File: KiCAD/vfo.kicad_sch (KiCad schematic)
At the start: 18 parts, among them Q1 J310, U1 Si5351A_Breakout, U2 MC1496

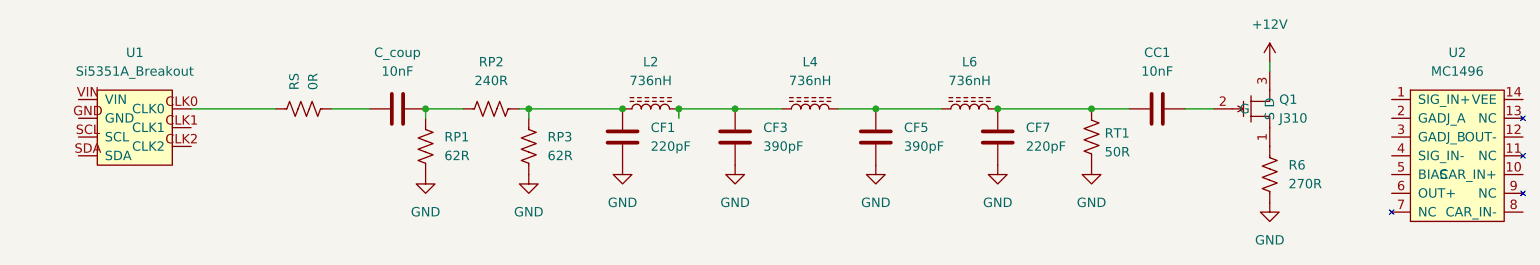
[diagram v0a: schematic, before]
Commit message: kicad: control-board sheets — buffer_keyer keyer body, arduino SPI labels, custom-symbol plan
- buffer_keyer.kicad_sch: place MC1496 keyer support components
  (carrier divider R11/R12, modulator port R3, emitter-degen Re,
  modulator coupling C1, VEE bypass C5, R2 Iee, bypass network),
  MCP4921 envelope DAC U4 with reconstruction cap C3, terminal
  blocks J1/J2/J3 for +5V/+12V/-90V/VEE input, hierarchical labels
  for VFO_OUT, SCK, MOSI, CS_DAC.
- arduino.kicad_sch: add SCK and MOSI hierarchical outputs for SPI
  link to MCP4921. CS_DAC still TODO.
- vfo.kicad_sch + KiCAD.kicad_sch: minor edits, sheet pin updates.
- Documentation/kicad_custom_symbols.md: new doc — pattern and plan
  for project-local xmitter:Metro_ESP32S3 symbol to replace the
  cluttered stock symbol (~30 pins → 10 pins, project-named).
- VFO_Keyer_Order.xlsx: small status updates.
- xmitter_prj/keyer.sch: minor cleanup.
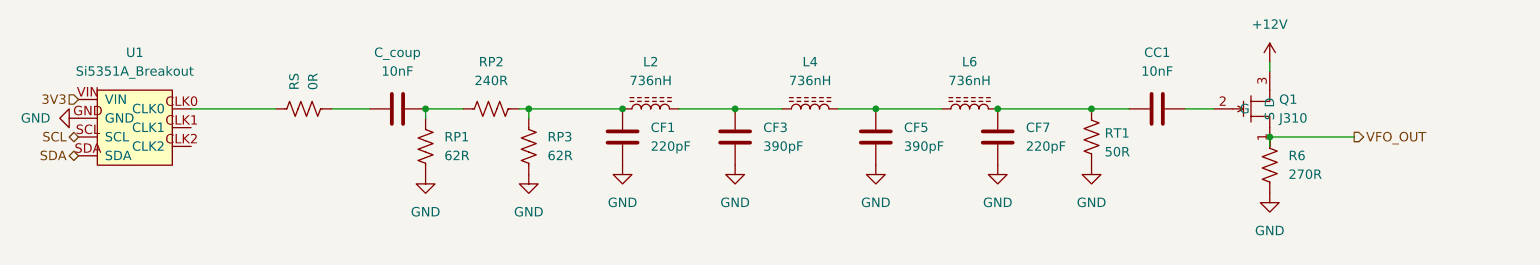
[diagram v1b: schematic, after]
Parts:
- removed U2: MC1496, Package_DIP:DIP-14_W7.62mm, symbol xmitter:MC1496
- L2, L4, L6: footprint Inductor_THT:L_Toroid_Horizontal_D14.0mm_P20.32mm -> Inductor_THT:L_Toroid_Horizontal_D17.3mm_P15.24mm_Bourns_2000
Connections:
- net GND: now also U1.GND
- net VFO_OUT: now reaches Q1.1 (S), R6.1
- net SCL: now reaches U1.SCL
- net SDA: now reaches U1.SDA
- net 3V3: now reaches U1.VIN
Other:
- moved on the sheet: R6
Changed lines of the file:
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@@
-	)
-	(junction
-		(at 124.46 62.23)
-		(diameter 0)
-		(color 0 0 0 0)
 	)
 	(junction
@@
 	)
 	(junction
+		(at 204.47 66.04)
+		(diameter 0)
+		(color 0 0 0 0)
+	)
+	(junction
 		(at 180.34 62.23)
 		(diameter 0)
@@
 	(wire
 		(pts
-			(xy 124.46 62.23) (xy 124.46 63.5)
+			(xy 104.14 62.23) (xy 116.84 62.23)
 		)
 		(stroke
@@
 	(wire
 		(pts
-			(xy 104.14 62.23) (xy 116.84 62.23)
+			(xy 151.13 62.23) (xy 160.02 62.23)
 		)
 		(stroke
@@
 	(wire
 		(pts
-			(xy 151.13 62.23) (xy 160.02 62.23)
+			(xy 204.47 55.88) (xy 204.47 57.15)
 		)
 		(stroke
@@
 	(wire
 		(pts
-			(xy 204.47 55.88) (xy 204.47 57.15)
+			(xy 204.47 66.04) (xy 204.47 67.31)
 		)
 		(stroke
@@
 		)
 	)
+	(wire
+		(pts
+			(xy 204.47 66.04) (xy 215.9 66.04)
+		)
+		(stroke
+			(width 0)
+			(type default)
+		)
+	)
+	(hierarchical_label "3V3"
+		(shape input)
+		(at 43.18 60.96 180)
+		(effects
+			(font
+				(size 1.27 1.27)
+			)
+			(justify right)
+		)
+	)
+	(hierarchical_label "SDA"
+		(shape bidirectional)
+		(at 43.18 68.58 180)
+		(effects
+			(font
+				(size 1.27 1.27)
+			)
+			(justify right)
+		)
+	)
+	(hierarchical_label "VFO_OUT"
+		(shape output)
+		(at 215.9 66.04 0)
+		(effects
+			(font
+				(size 1.27 1.27)
+			)
+			(justify left)
+		)
+	)
+	(hierarchical_label "SCL"
+		(shape bidirectional)
+		(at 43.18 66.04 180)
+		(effects
+			(font
+				(size 1.27 1.27)
+			)
+			(justify right)
+		)
+	)
 	(symbol
 		(lib_id "power:GND")
@@
 	)
 	(symbol
-		(lib_id "xmitter:MC1496")
-		(at 229.87 68.58 0)
-		(unit 1)
-		(body_style 1)
-		(exclude_from_sim no)
-		(in_bom yes)
-		(on_board yes)
-		(in_pos_files yes)
-		(dnp no)
-		(fields_autoplaced yes)
-		(property "Reference" "U2"
-			(at 229.87 54.61 0)
-			(show_name no)
-			(do_not_autoplace no)
-			(effects
-				(font
-					(size 1.27 1.27)
-				)
-			)
-		)
-		(property "Value" "MC1496"
-			(at 229.87 57.15 0)
-			(show_name no)
-			(do_not_autoplace no)
-			(effects
-				(font
-					(size 1.27 1.27)
-				)
-			)
-		)
-		(property "Footprint" "Package_DIP:DIP-14_W7.62mm"
-			(at 229.87 68.58 0)
-			(hide yes)
-			(show_name no)
-			(do_not_autoplace no)
-			(effects
-				(font
-					(size 1.27 1.27)
-				)
-			)
-		)
-		(property "Datasheet" "https://www.onsemi.com/pdf/datasheet/mc1496-d.pdf"
-			(at 229.87 68.58 0)
-			(hide yes)
-			(show_name no)
-			(do_not_autoplace no)
-			(effects
-				(font
-					(size 1.27 1.27)
-				)
-			)
-		)
-		(property "Description" "Balanced Modulator/Demodulator, DIP-14"
-			(at 229.87 68.58 0)
-			(hide yes)
-			(show_name no)
-			(do_not_autoplace no)
-			(effects
-				(font
-					(size 1.27 1.27)
-				)
-			)
-		)
-		(property "Manufacturer" "onsemi"
-			(at 229.87 68.58 0)
-			(hide yes)
-			(show_name no)
-			(do_not_autoplace no)
-			(effects
-				(font
-					(size 1.27 1.27)
-				)
-			)
-		)
-		(property "MPN" "MC1496P"
-			(at 229.87 68.58 0)
-			(hide yes)
-			(show_name no)
-			(do_not_autoplace no)
-			(effects
-				(font
-					(size 1.27 1.27)
-				)
-			)
-		)
-		(pin "9"
-		)
-		(pin "14"
-		)
-		(pin "6"
-		)
-		(pin "13"
-		)
-		(pin "11"
-		)
-		(pin "10"
-		)
-		(pin "12"
-		)
-		(pin "1"
-		)
-		(pin "2"
-		)
-		(pin "4"
-		)
-		(pin "3"
-		)
-		(pin "5"
-		)
-		(pin "7"
-		)
-		(pin "8"
-		)
-		(instances
-			(project "KiCAD"
-				(path "/d3de40b8-856b-4fbd-829c-f45ffcd55742/c08cbce4-6e06-48f3-b334-a48b1cc09989"
-					(reference "U2")
-					(unit 1)
-				)
-			)
-		)
-	)
-	(symbol
 		(lib_id "Device:C")
 		(at 132.08 66.04 0)
@@
 			)
 		)
-		(property "Footprint" "Inductor_THT:L_Toroid_Horizontal_D14.0mm_P20.32mm"
+		(property "Footprint" "Inductor_THT:L_Toroid_Horizontal_D17.3mm_P15.24mm_Bourns_2000"
 			(at 163.83 62.23 0)
 			(hide yes)
@@
 	(symbol
 		(lib_id "power:GND")
-		(at 204.47 74.93 0)
+		(at 204.47 73.66 0)
 		(unit 1)
 		(body_style 1)
@@
 		(fields_autoplaced yes)
 		(property "Reference" "#PWR07"
-			(at 204.47 81.28 0)
+			(at 204.47 80.01 0)
 			(hide yes)
 			(show_name no)
@@
 		)
 		(property "Value" "GND"
-			(at 204.47 80.01 0)
+			(at 204.47 78.74 0)
 			(show_name no)
 			(do_not_autoplace no)
@@
 		)
 		(property "Footprint" ""
-			(at 204.47 74.93 0)
+			(at 204.47 73.66 0)
 			(hide yes)
 			(show_name no)
@@
 		)
 		(property "Datasheet" ""
-			(at 204.47 74.93 0)
+			(at 204.47 73.66 0)
 			(hide yes)
 			(show_name no)
@@
 		)
 		(property "Description" "Power symbol creates a global label with name \"GND\" , ground"
-			(at 204.47 74.93 0)
+			(at 204.47 73.66 0)
 			(hide yes)
 			(show_name no)
@@
 	(symbol
 		(lib_id "Device:R_US")
-		(at 204.47 71.12 0)
+		(at 204.47 69.85 0)
 		(unit 1)
 		(body_style 1)
@@
 		(fields_autoplaced yes)
 		(property "Reference" "R6"
-			(at 207.01 69.8499 0)
+			(at 207.01 68.5799 0)
 			(show_name no)
 			(do_not_autoplace no)
@@
 		)
 		(property "Value" "270R"
-			(at 207.01 72.3899 0)
+			(at 207.01 71.1199 0)
 			(show_name no)
 			(do_not_autoplace no)
@@
 		)
 		(property "Footprint" "Resistor_THT:R_Axial_DIN0207_L6.3mm_D2.5mm_P10.16mm_Horizontal"
-			(at 205.486 71.374 90)
+			(at 205.486 70.104 90)
 			(hide yes)
 			(show_name no)
@@
 		)
 		(property "Datasheet" ""
-			(at 204.47 71.12 0)
+			(at 204.47 69.85 0)
 			(hide yes)
 			(show_name no)
@@
 		)
 		(property "Description" "metal film"
-			(at 204.47 71.12 0)
+			(at 204.47 69.85 0)
 			(hide yes)
 			(show_name no)
@@
 		)
 		(property "power" "1/4W"
-			(at 204.47 71.12 0)
+			(at 204.47 69.85 0)
 			(hide yes)
 			(show_name no)
@@
 			)
 		)
-		(property "Footprint" "Inductor_THT:L_Toroid_Horizontal_D14.0mm_P20.32mm"
+		(property "Footprint" "Inductor_THT:L_Toroid_Horizontal_D17.3mm_P15.24mm_Bourns_2000"
 			(at 142.24 62.23 0)
 			(hide yes)
@@
 			)
 		)
-		(property "Footprint" "Inductor_THT:L_Toroid_Horizontal_D14.0mm_P20.32mm"
+		(property "Footprint" "Inductor_THT:L_Toroid_Horizontal_D17.3mm_P15.24mm_Bourns_2000"
 			(at 120.65 62.23 0)
 			(hide yes)
@@
 					(unit 1)
 				)
+			)
+		)
+	)
+	(symbol
+		(lib_id "power:GND")
+		(at 43.18 63.5 270)
+		(unit 1)
+		(body_style 1)
+		(exclude_from_sim no)
+		(in_bom yes)
+		(on_board yes)
+		(in_pos_files yes)
+		(dnp no)
+		(fields_autoplaced yes)
+		(property "Reference" "#PWR023"
+			(at 36.83 63.5 0)
+			(hide yes)
+			(show_name no)
+			(do_not_autoplace no)
+			(effects
+				(font
+					(size 1.27 1.27)
+				)
+			)
+		)
+		(property "Value" "GND"
+			(at 39.37 63.4999 90)
+			(show_name no)
+			(do_not_autoplace no)
+			(effects
+				(font
+					(size 1.27 1.27)
+				)
+				(justify right)
+			)
+		)
+		(property "Footprint" ""
+			(at 43.18 63.5 0)
+			(hide yes)
+			(show_name no)
+			(do_not_autoplace no)
+			(effects
+				(font
+					(size 1.27 1.27)
+				)
+			)
+		)
+		(property "Datasheet" ""
+			(at 43.18 63.5 0)
+			(hide yes)
+			(show_name no)
+			(do_not_autoplace no)
+			(effects
+				(font
+					(size 1.27 1.27)
+				)
+			)
+		)
+		(property "Description" "Power symbol creates a global label with name \"GND\" , ground"
+			(at 43.18 63.5 0)
+			(hide yes)
+			(show_name no)
+			(do_not_autoplace no)
+			(effects
+				(font
+					(size 1.27 1.27)
+				)
+			)
+		)
+		(pin "1"
+		)
+		(instances
+			(project "KiCAD"
+				(path "/d3de40b8-856b-4fbd-829c-f45ffcd55742/c08cbce4-6e06-48f3-b334-a48b1cc09989"
+					(reference "#PWR023")
+					(unit 1)
+				)

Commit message: kicad: rename VFO_OUT signals to direction-named labels (RAW_RF_*, MOD_RF_*)
The 14 MHz unmodulated signal between VFO and buffer_keyer was
labeled "VFO_OUT" on BOTH sheets, which was directionally ambiguous.
The differential post-modulation outputs of the LM7171 stage were
also labeled "VFO_OUT+/-", which was wrong — by that point in the
chain the signal is keyed/modulated, not raw VFO.

Renames:
- vfo.kicad_sch: hier label VFO_OUT (output) -> RAW_RF_OUT
- buffer_keyer.kicad_sch: hier label VFO_OUT (input) -> RAW_RF_IN
- buffer_keyer.kicad_sch: VFO_OUT+ (output) -> MOD_RF_OUT+
- buffer_keyer.kicad_sch: VFO_OUT- (output) -> MOD_RF_OUT- (also fixed
  a typo where the minus side was mistakenly named MOD_RF-OUT- with a
  hyphen between RF and OUT)
- KiCAD.kicad_sch (root): two sheet pins renamed to match
  (VFO sheet -> RAW_RF_OUT; VFO_Buffer_keyer sheet -> RAW_RF_IN). Pin
  coordinates and UUIDs preserved so existing root-sheet wiring stays
  attached.

Also added Documentation/Components/lm7171.pdf (TI datasheet) - was
already referenced in the supply-voltage compliance audit but hadn't
been committed.
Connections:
- net VFO_OUT renamed RAW_RF_OUT
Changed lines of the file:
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@@
 		)
 	)
-	(hierarchical_label "VFO_OUT"
+	(hierarchical_label "RAW_RF_OUT"
 		(shape output)
 		(at 215.9 66.04 0)

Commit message: kicad: re-architect I2C bus distribution via STEMMA QT to Si5351 hub
Move I2C (SDA/SCL) and +3.3V distribution from arduino-sheet-origin to
vfo-sheet-origin, matching the physical plan: STEMMA QT cable carries
I2C + 3.3V from Metro to Si5351 breakout (off-schematic), and from the
Si5351 breakout's 0.1" header the bus is distributed via PCB traces to
other I2C devices (MCP4728, future MCP23017 for LCD).

Per-file changes:

- xmitter.kicad_sym (Metro_ESP32S3 symbol): D2/D3 relabeled from
  D2/SDA, D3/SCL to D2/FREQ_A, D3/FREQ_B (input type). Aligns with
  firmware/main/pin_map.h which already uses D2/D3 for the FREQ encoder
  quadrature inputs. The real Metro's dedicated SDA/SCL pins (GPIO
  47/48) are not exposed on this custom symbol; I2C goes off-board via
  STEMMA QT.
- arduino.kicad_sch: removed SDA/SCL/3V3 hier labels (no longer the
  source of these signals). Added +3.3V power port at Metro 3V3 pin
  for ERC cleanliness. Added text note explaining STEMMA QT routing.
- vfo.kicad_sch: 3V3, SDA, SCL hier labels changed direction to output
  (Si5351 breakout is now the source).
- buffer_keyer.kicad_sch: added 3V3 (input) hier label at (48.26,
  134.62) alongside existing SDA/SCL inputs. Existing +3.3V power port
  at U8 VIN stays for now; user will need to wire the new label to
  the +3.3V net inside KiCad (or replace the power port with the label).

tools/:
- rewrite_metro_symbol.py: pin list updated, wire-deletion code
  REMOVED (it was unconditionally wiping wires on every run — only
  correct on the first conversion).
- rewire_arduino_for_stemma.py: one-shot script for the arduino sheet
  changes.
- add_3v3_label_buffer_keyer.py: one-shot script for the new 3V3 hier
  label.

Root sheet update + sheet-pin sync + cross-sheet wiring deferred to
user (needs KiCad GUI's "Import Sheet Pins" feature).
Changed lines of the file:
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@@
 	)
 	(hierarchical_label "3V3"
-		(shape input)
+		(shape output)
 		(at 43.18 60.96 180)
 		(effects
@@
 	)
 	(hierarchical_label "SDA"
-		(shape bidirectional)
+		(shape output)
 		(at 43.18 68.58 180)
 		(effects
@@
 	)
 	(hierarchical_label "SCL"
-		(shape bidirectional)
+		(shape output)
 		(at 43.18 66.04 180)
 		(effects
